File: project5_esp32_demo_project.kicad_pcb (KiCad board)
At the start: 4 copper layers, 0 parts

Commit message: 1.3.7 Import schematic into the layout editor
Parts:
- added C1: 0.1u, Capacitor_SMD:C_0805_2012Metric, F.Cu at (149.4, 80.3)
- added C10: 0.1u, Capacitor_SMD:C_0805_2012Metric, F.Cu at (130.0, 107.6)
- added C11: 1u, Capacitor_SMD:C_0805_2012Metric, F.Cu at (130.0, 110.6)
- added C12: 10u, ESP32_demo_project:T491A106K010AT7280, F.Cu at (143.9, 111.5)
- added C13: 0.1u, Capacitor_SMD:C_0805_2012Metric, F.Cu at (130.0, 113.7)
- added C14: 0.1u, Capacitor_SMD:C_0805_2012Metric, F.Cu at (130.0, 116.7)
- added C15: 0.1u, Capacitor_SMD:C_0805_2012Metric, F.Cu at (150.9, 104.6)
- added C16: 0.1u, Capacitor_SMD:C_0805_2012Metric, F.Cu at (150.9, 107.6)
- added C18: 0.1u, Capacitor_SMD:C_0805_2012Metric, F.Cu at (150.9, 110.6)
- added C2: 0.1u, Capacitor_SMD:C_0805_2012Metric, F.Cu at (149.4, 83.3)
- added C20: 0.1u, Capacitor_SMD:C_0805_2012Metric, F.Cu at (150.9, 113.7)
- added C21: 0.1u, Capacitor_SMD:C_0805_2012Metric, F.Cu at (160.8, 92.5)
- added C22: 1u, Capacitor_SMD:C_0805_2012Metric, F.Cu at (160.8, 95.5)
- added C3: 10u, ESP32_demo_project:T491A106K010AT7280, F.Cu at (146.9, 95.2)
- added C4: 10u, ESP32_demo_project:T491A106K010AT7280, F.Cu at (146.9, 98.6)
- added C5: 0.1u, Capacitor_SMD:C_0805_2012Metric, F.Cu at (149.4, 86.3)
- added C6: 1u, Capacitor_SMD:C_0805_2012Metric, F.Cu at (149.4, 89.3)
- added C7: 10u, ESP32_demo_project:T491A106K010AT7280, F.Cu at (143.9, 104.8)
- added C8: 0.1u, Capacitor_SMD:C_0805_2012Metric, F.Cu at (130.0, 104.6)
- added C9: 4.7u, ESP32_demo_project:T491A106K010AT7280, F.Cu at (143.9, 108.1)
- added F1: 0ZCH0110AF2E, ESP32_demo_project:0ZCH0110AF2E, F.Cu at (141.2, 95.7)
- added J1: SS-52400-002, ESP32_demo_project:SS-52400-002, F.Cu at (130.3, 87.9)
- added J4: Conn_01x04_Pin, Connector_PinHeader_2.54mm:PinHeader_1x04_P2.54mm_Vertical, F.Cu at (160.8, 81.1)
- added J5: Conn_01x05_Pin, Connector_PinHeader_2.54mm:PinHeader_1x05_P2.54mm_Vertical, F.Cu at (165.4, 81.1)
- added Q2: BC817, Package_TO_SOT_SMD:SOT-23, F.Cu at (156.1, 81.0)
- added Q3: BC817, Package_TO_SOT_SMD:SOT-23, F.Cu at (156.1, 85.5)
- added R1: 10K, Resistor_SMD:R_0805_2012Metric, F.Cu at (140.6, 80.3)
- added R10: 470, Resistor_SMD:R_0805_2012Metric, F.Cu at (145.0, 92.1)
- added R11: 1k, Resistor_SMD:R_0805_2012Metric, F.Cu at (134.4, 104.6)
- added R12: 22K1, Resistor_SMD:R_0805_2012Metric, F.Cu at (134.4, 107.5)
- added R13: 47K5, Resistor_SMD:R_0805_2012Metric, F.Cu at (134.4, 110.5)
- added R14: 470, Resistor_SMD:R_0805_2012Metric, F.Cu at (134.4, 113.4)
- added R15: 50, Resistor_SMD:R_0805_2012Metric, F.Cu at (134.4, 116.4)
- added R16: 50, Resistor_SMD:R_0805_2012Metric, F.Cu at (138.8, 104.6)
- added R17: 50, Resistor_SMD:R_0805_2012Metric, F.Cu at (138.8, 107.5)
- added R18: 470, Resistor_SMD:R_0805_2012Metric, F.Cu at (138.8, 110.5)
- added R19: 10K, Resistor_SMD:R_0805_2012Metric, F.Cu at (138.8, 113.4)
- added R2: 10K, Resistor_SMD:R_0805_2012Metric, F.Cu at (140.6, 83.2)
- added R20: 50, Resistor_SMD:R_0805_2012Metric, F.Cu at (138.8, 116.4)
- added R23: 10K, Resistor_SMD:R_0805_2012Metric, F.Cu at (155.4, 104.6)
- added R24: 4K7, Resistor_SMD:R_0805_2012Metric, F.Cu at (155.4, 107.5)
- added R25: 4K7, Resistor_SMD:R_0805_2012Metric, F.Cu at (155.4, 110.5)
- added R26: 2K, Resistor_SMD:R_0805_2012Metric, F.Cu at (159.8, 104.6)
- added R27: 1M, Resistor_SMD:R_0805_2012Metric, F.Cu at (159.8, 107.5)
- added R28: 2K, Resistor_SMD:R_0805_2012Metric, F.Cu at (159.8, 110.5)
- added R29: 1M, Resistor_SMD:R_0805_2012Metric, F.Cu at (164.2, 104.6)
- added R3: 5K1, Resistor_SMD:R_0805_2012Metric, F.Cu at (140.6, 86.2)
- added R30: 10K, Resistor_SMD:R_0805_2012Metric, F.Cu at (164.2, 107.5)
- added R31: 100K, Resistor_SMD:R_0805_2012Metric, F.Cu at (164.2, 110.5)
- added R32: 10K, Resistor_SMD:R_0805_2012Metric, F.Cu at (155.8, 89.2)
- added R33: 10K, Resistor_SMD:R_0805_2012Metric, F.Cu at (155.8, 92.1)
- added R34: 10K, Resistor_SMD:R_0805_2012Metric, F.Cu at (155.8, 95.1)
- added R4: 5K1, Resistor_SMD:R_0805_2012Metric, F.Cu at (140.6, 89.1)
- added R5: 2K, Resistor_SMD:R_0805_2012Metric, F.Cu at (140.6, 92.1)
- added R6: 20K, Resistor_SMD:R_0805_2012Metric, F.Cu at (145.0, 80.3)
- added R7: 470, Resistor_SMD:R_0805_2012Metric, F.Cu at (145.0, 83.2)
- added R8: 470, Resistor_SMD:R_0805_2012Metric, F.Cu at (145.0, 86.2)
- added R9: 470, Resistor_SMD:R_0805_2012Metric, F.Cu at (145.0, 89.1)
- added TP1: Test MOSI, TestPoint:TestPoint_Pad_D1.0mm, F.Cu at (126.3, 104.6)
- added TP2: Test MISO, TestPoint:TestPoint_Pad_D1.0mm, F.Cu at (126.3, 107.7)
- added TP3: Test SCLK, TestPoint:TestPoint_Pad_D1.0mm, F.Cu at (126.3, 110.7)
- added TP4: Test CS_SD, TestPoint:TestPoint_Pad_D1.0mm, F.Cu at (126.3, 113.8)
- added TP5: Test CS, TestPoint:TestPoint_Pad_D1.0mm, F.Cu at (126.3, 116.8)
- added U5: USBLC6-2SC6, Package_TO_SOT_SMD:SOT-23-6, F.Cu at (143.6, 115.6)
- added VR1: LM1117MPX-3.3, ESP32_demo_project:LM1117MPX-3.3, F.Cu at (130.0, 97.1)

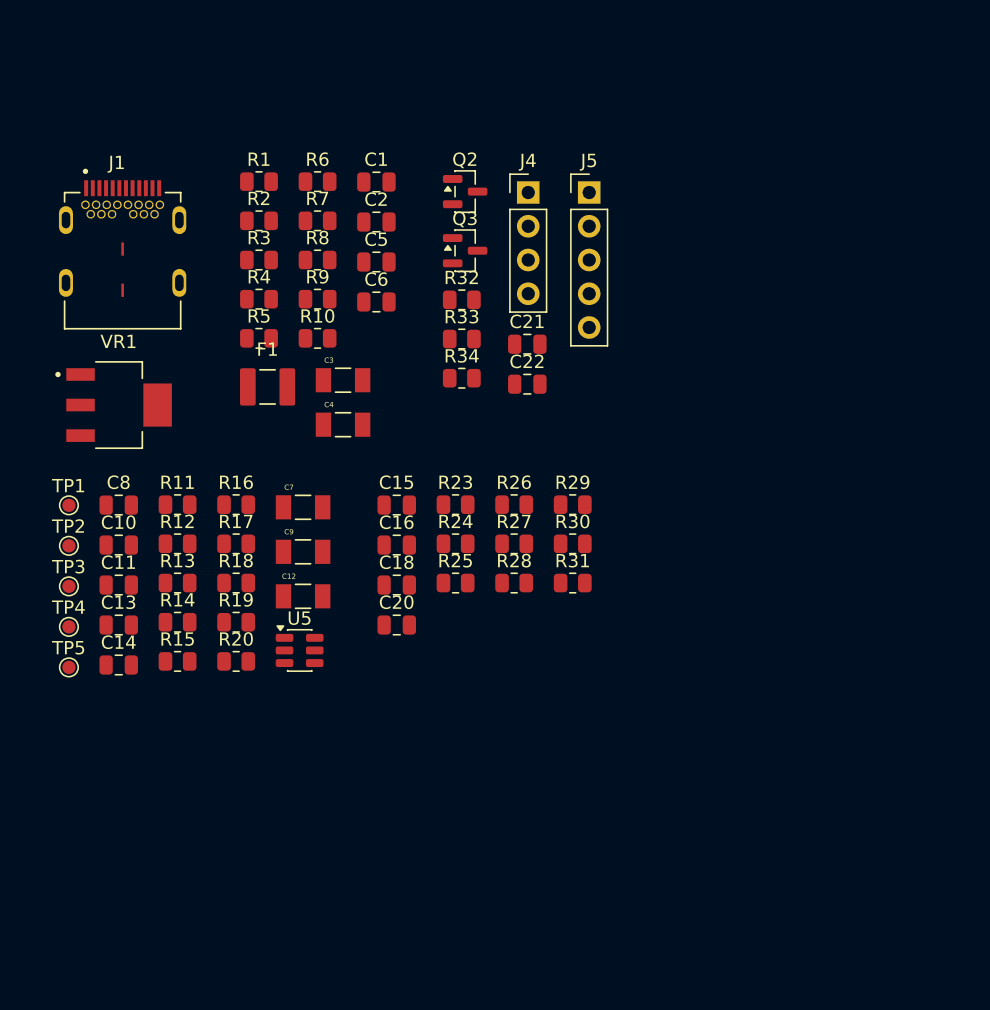
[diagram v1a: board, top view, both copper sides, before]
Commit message: 1.3.9 Bring remaining components to the layout editor
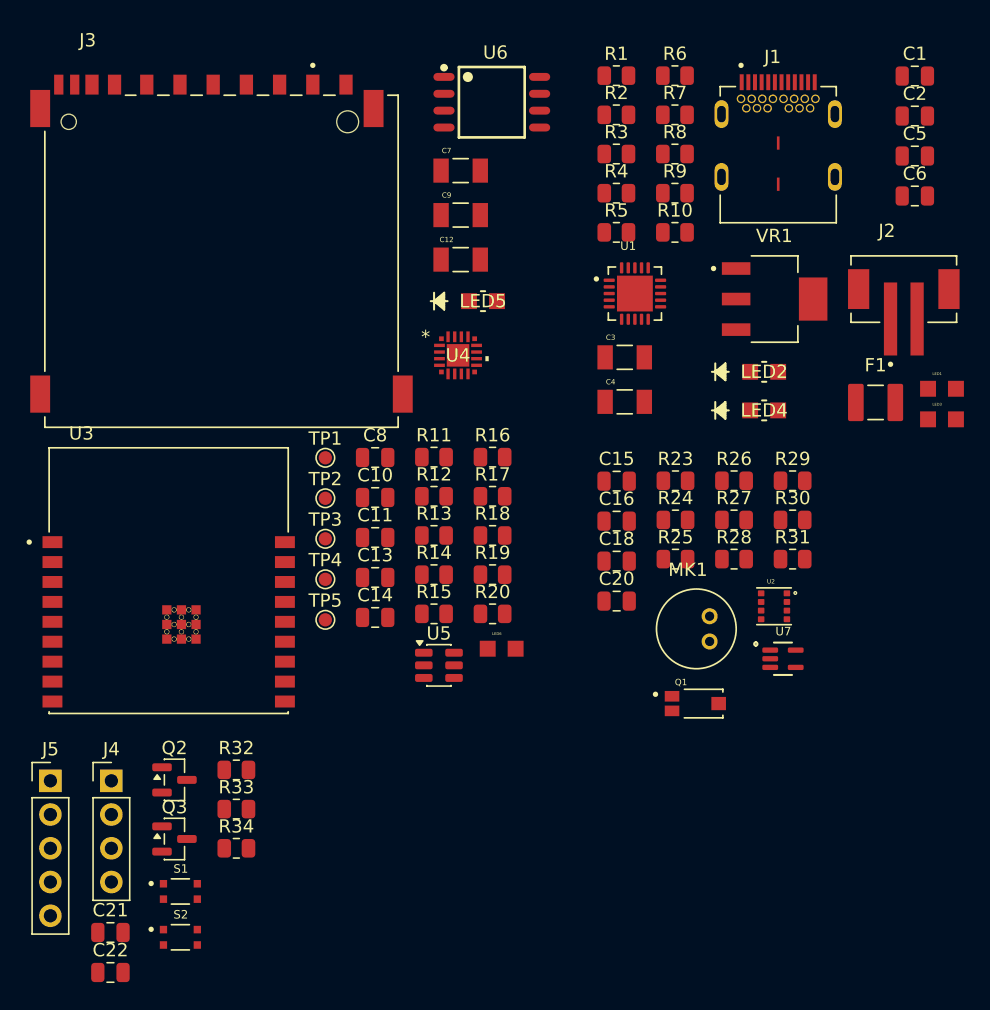
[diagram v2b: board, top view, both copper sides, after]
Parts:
- added J2: B2B-PH-SM4-TB, ESP32_demo_project:B2B-PH-SM4-TB, F.Cu at (189.1, 88.4)
- added J3: GSD090012SEU, ESP32_demo_project:GSD090012SEU, F.Cu at (137.7, 86.3)
- added LED1: LTST-C170KRKT, ESP32_demo_project:LTST-C170KRKT, F.Cu at (192.0, 95.9)
- added LED2: LTST-C170GKT, ESP32_demo_project:LTST-C170GKT, F.Cu at (178.6, 94.6)
- added LED3: LTST-C170TBKT, ESP32_demo_project:LTST-C170TBKT, F.Cu at (192.0, 98.2)
- added LED4: LTST-C170GKT, ESP32_demo_project:LTST-C170GKT, F.Cu at (178.6, 97.5)
- added LED5: LTST-C170GKT, ESP32_demo_project:LTST-C170GKT, F.Cu at (157.4, 89.3)
- added LED6: LTST-C170KRKT, ESP32_demo_project:LTST-C170KRKT, F.Cu at (158.8, 115.4)
- added MK1: CMC-5042PF-AC, ESP32_demo_project:CMC-5042PF-AC, F.Cu at (173.5, 113.9)
- added Q1: TEMT6000X01, ESP32_demo_project:TEMT6000X01, F.Cu at (173.4, 119.6)
- added S1: Boot, ESP32_demo_project:USLPT2819DT2TR, F.Cu at (134.6, 133.7)
- added S2: Reset, ESP32_demo_project:USLPT2819DT2TR, F.Cu at (134.6, 137.2)
- added U1: MCP73871-2CAI_ML, ESP32_demo_project:MCP73871-2CAI_ML, F.Cu at (168.9, 88.7)
- added U2: BME280, ESP32_demo_project:BME280, F.Cu at (179.3, 112.2)
- added U3: ESP32-C3-WROOM-02-H4, ESP32_demo_project:ESP32-C3-WROOM-02-H4, F.Cu at (133.8, 110.3)
- added U4: CP2102N-Axx-xQFN20, ESP32_demo_project:QFN20_CP2102N_SIL, F.Cu at (155.6, 93.3)
- added U6: W25Q32JVSSIQ, ESP32_demo_project:W25Q32JVSSIQ, F.Cu at (158.1, 74.3)
- added U7: MAX4466EXK, ESP32_demo_project:MAX4466EXK, F.Cu at (180.0, 116.2)
- moved J5 60.1 mm to (124.9, 125.4)
- moved C21 54.3 mm to (129.4, 136.8)
- moved C22 54.3 mm to (129.4, 139.8)
- moved J4 54.3 mm to (129.5, 125.4)
- moved VR1 50.0 mm to (179.4, 89.1)
- moved J1 50.0 mm to (179.7, 79.9)
- moved Q2 49.4 mm to (134.2, 125.3)
- moved Q3 49.4 mm to (134.2, 129.8)
- moved F1 45.8 mm to (187.0, 96.9)
- moved C1 41.3 mm to (189.9, 72.3)
- moved C2 41.3 mm to (189.9, 75.3)
- moved C5 41.3 mm to (189.9, 78.3)
- moved C6 41.3 mm to (189.9, 81.3)
- moved R34 39.3 mm to (138.9, 130.5)
- moved R32 39.3 mm to (138.9, 124.6)
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
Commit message: 1.4.0 Main components placement
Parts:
- moved U3 49.9 mm to (91.4, 83.8)
- moved J3 36.9 mm to (123.8, 52.1)
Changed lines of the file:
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@@
 	(footprint "ESP32_demo_project:GSD090012SEU"
 		(layer "F.Cu")
-		(at 137.743 86.265)
+		(at 123.825 52.07)
 		(property "Reference" "J3"
 			(at -10.075 -16.635 0)
@@
 			(polygon
 				(pts
-					(xy 127.243 80.915) (xy 148.243 80.915) (xy 148.243 86.215) (xy 127.243 86.215)
+					(xy 113.325 46.72) (xy 134.325 46.72) (xy 134.325 52.02) (xy 113.325 52.02)
 				)
 			)
@@
 			(polygon
 				(pts
-					(xy 127.243 80.915) (xy 148.243 80.915) (xy 148.243 86.215) (xy 127.243 86.215)
+					(xy 113.325 46.72) (xy 134.325 46.72) (xy 134.325 52.02) (xy 113.325 52.02)
 				)
 			)
@@
 	(footprint "ESP32_demo_project:ESP32-C3-WROOM-02-H4"
 		(layer "F.Cu")
-		(at 133.768 110.31)
+		(at 91.44 83.82)
 		(property "Reference" "U3"
 			(at -6.575 -11.085 0)
@@
 			(polygon
 				(pts
-					(xy 124.768 100.31) (xy 142.768 100.31) (xy 142.768 106.31) (xy 124.768 106.31)
+					(xy 82.44 73.82) (xy 100.44 73.82) (xy 100.44 79.82) (xy 82.44 79.82)
 				)
 			)
@@
 			(polygon
 				(pts
-					(xy 124.768 100.31) (xy 142.768 100.31) (xy 142.768 106.31) (xy 124.768 106.31)
+					(xy 82.44 73.82) (xy 100.44 73.82) (xy 100.44 79.82) (xy 82.44 79.82)
 				)
 			)
@@
 			(polygon
 				(pts
-					(xy 124.768 100.31) (xy 142.768 100.31) (xy 142.768 106.31) (xy 124.768 106.31)
+					(xy 82.44 73.82) (xy 100.44 73.82) (xy 100.44 79.82) (xy 82.44 79.82)
 				)
 			)

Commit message: 1.4.1 Placement of subcircuits
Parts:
- moved LED4 162.3 mm to (28.6, 159.5)
- moved U3 162.1 mm to (245.1, 32.0)
- moved R10 159.4 mm to (29.3, 155.3)
- moved J2 153.5 mm to (38.4, 117.5)
- moved C1 145.5 mm to (53.0, 23.1)
- moved R3 145.5 mm to (30.5, 29.0)
- moved R4 145.5 mm to (30.5, 31.9)
- moved F1 145.5 mm to (50.1, 47.7)
- moved J1 145.5 mm to (42.7, 30.7)
- moved TP1 145.5 mm to (22.9, 179.2)
- moved TP2 145.5 mm to (22.9, 182.3)
- moved TP3 145.5 mm to (22.9, 185.3)
- moved TP4 145.5 mm to (22.9, 188.4)
- moved TP5 145.5 mm to (22.9, 191.4)
- moved J3 137.9 mm to (252.2, 102.5)
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
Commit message: 1.4.2 Components placement v2
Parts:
- moved TP1 206.1 mm to (192.2, 61.7)
- moved TP2 206.0 mm to (192.2, 65.0)
- moved TP3 206.0 mm to (192.2, 68.0)
- moved TP4 206.0 mm to (192.2, 71.1)
- moved TP5 206.0 mm to (192.2, 74.1)
- moved LED4 181.0 mm to (182.8, 64.7), turned to 90 degrees
- moved R10 171.0 mm to (175.5, 66.7)
- moved MK1 151.7 mm to (150.8, 66.9)
- moved C20 151.4 mm to (158.8, 77.2)
- moved C18 149.2 mm to (153.9, 72.5)
- moved C16 144.4 mm to (149.7, 72.2)
- moved Q1 142.9 mm to (189.2, 101.9)
- moved U7 142.8 mm to (154.1, 77.9)
- moved R3 141.6 mm to (159.5, 87.3)
- moved R4 138.6 mm to (159.5, 82.6), turned to 180 degrees
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
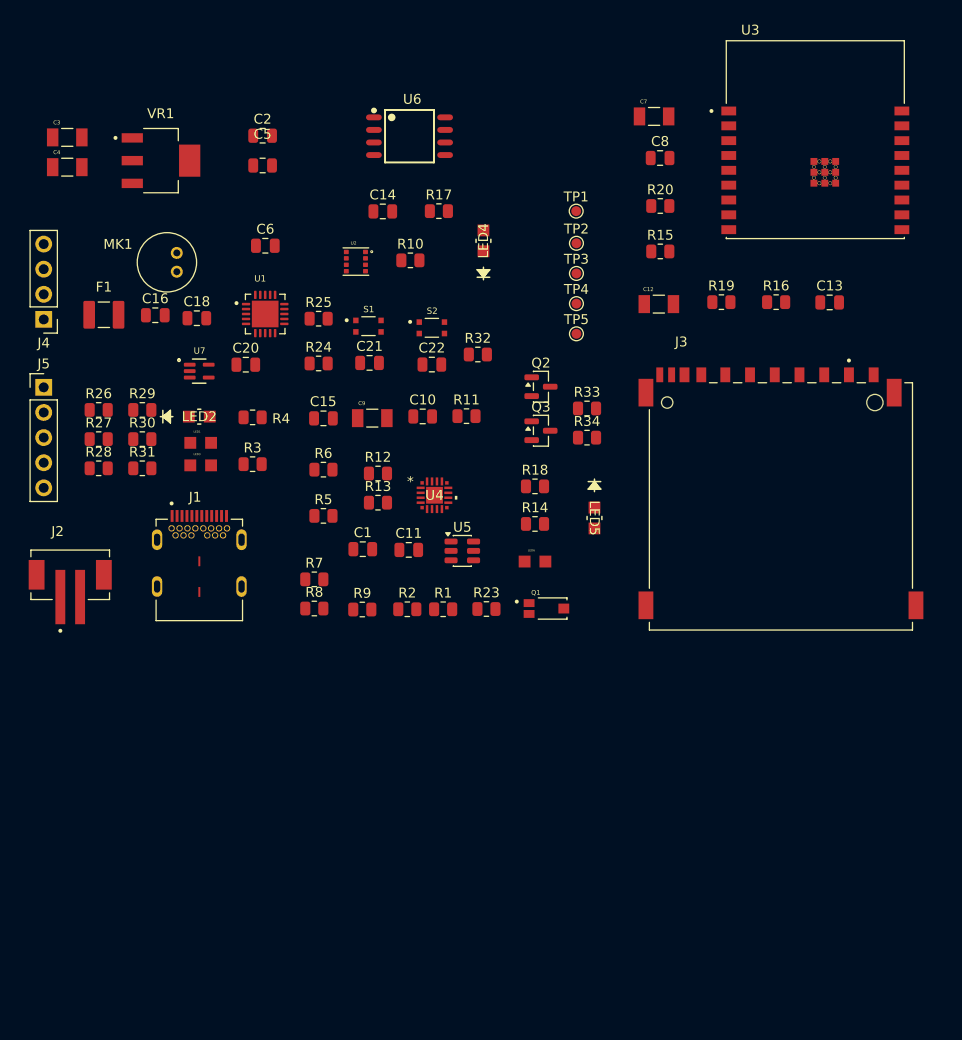
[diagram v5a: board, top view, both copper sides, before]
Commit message: 1.4.3 Draw the edge cut (rough board outline)
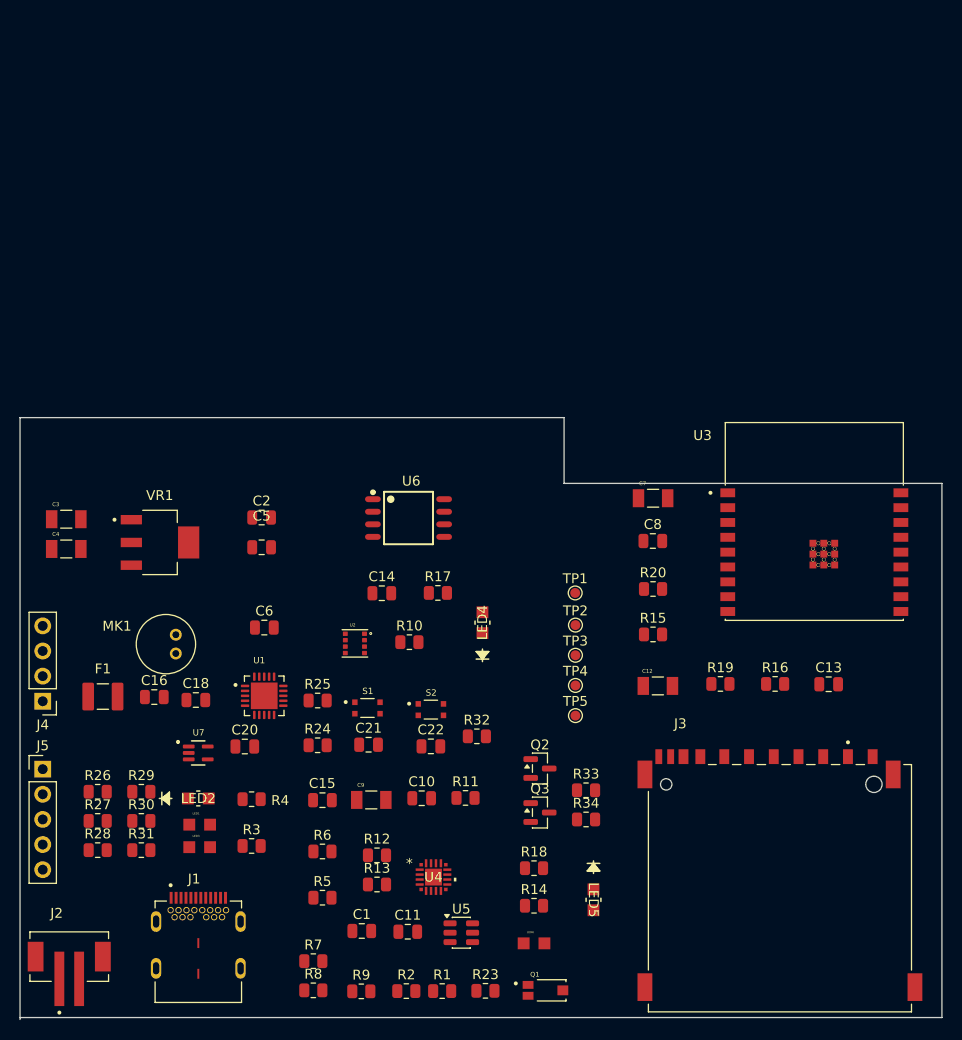
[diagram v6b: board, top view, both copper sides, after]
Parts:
- moved R15 38.7 mm to (200.0, 104.5)
- moved C8 38.7 mm to (200.0, 95.1)
- moved R20 38.7 mm to (200.0, 99.9)
- moved C10 38.6 mm to (176.6, 121.1)
- moved C13 38.6 mm to (217.8, 109.6)
- moved C15 38.6 mm to (166.6, 121.3)
- moved C18 38.6 mm to (153.8, 111.2)
- moved C21 38.6 mm to (171.2, 115.7)
- moved C6 38.6 mm to (160.7, 103.8)
- moved C9 38.6 mm to (171.5, 121.3)
- moved J1 38.6 mm to (154.0, 138.3)
- moved J2 38.6 mm to (141.0, 137.1)
- moved J3 38.6 mm to (212.8, 130.2)
- moved J4 38.6 mm to (138.3, 111.3)
- moved LED3 38.6 mm to (154.2, 126.0)
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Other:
- board outline added: 93.2 x 60.8 mm
